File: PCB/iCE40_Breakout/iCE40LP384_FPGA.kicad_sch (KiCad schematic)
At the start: 15 parts, among them U1 ICE40LP384-SG32

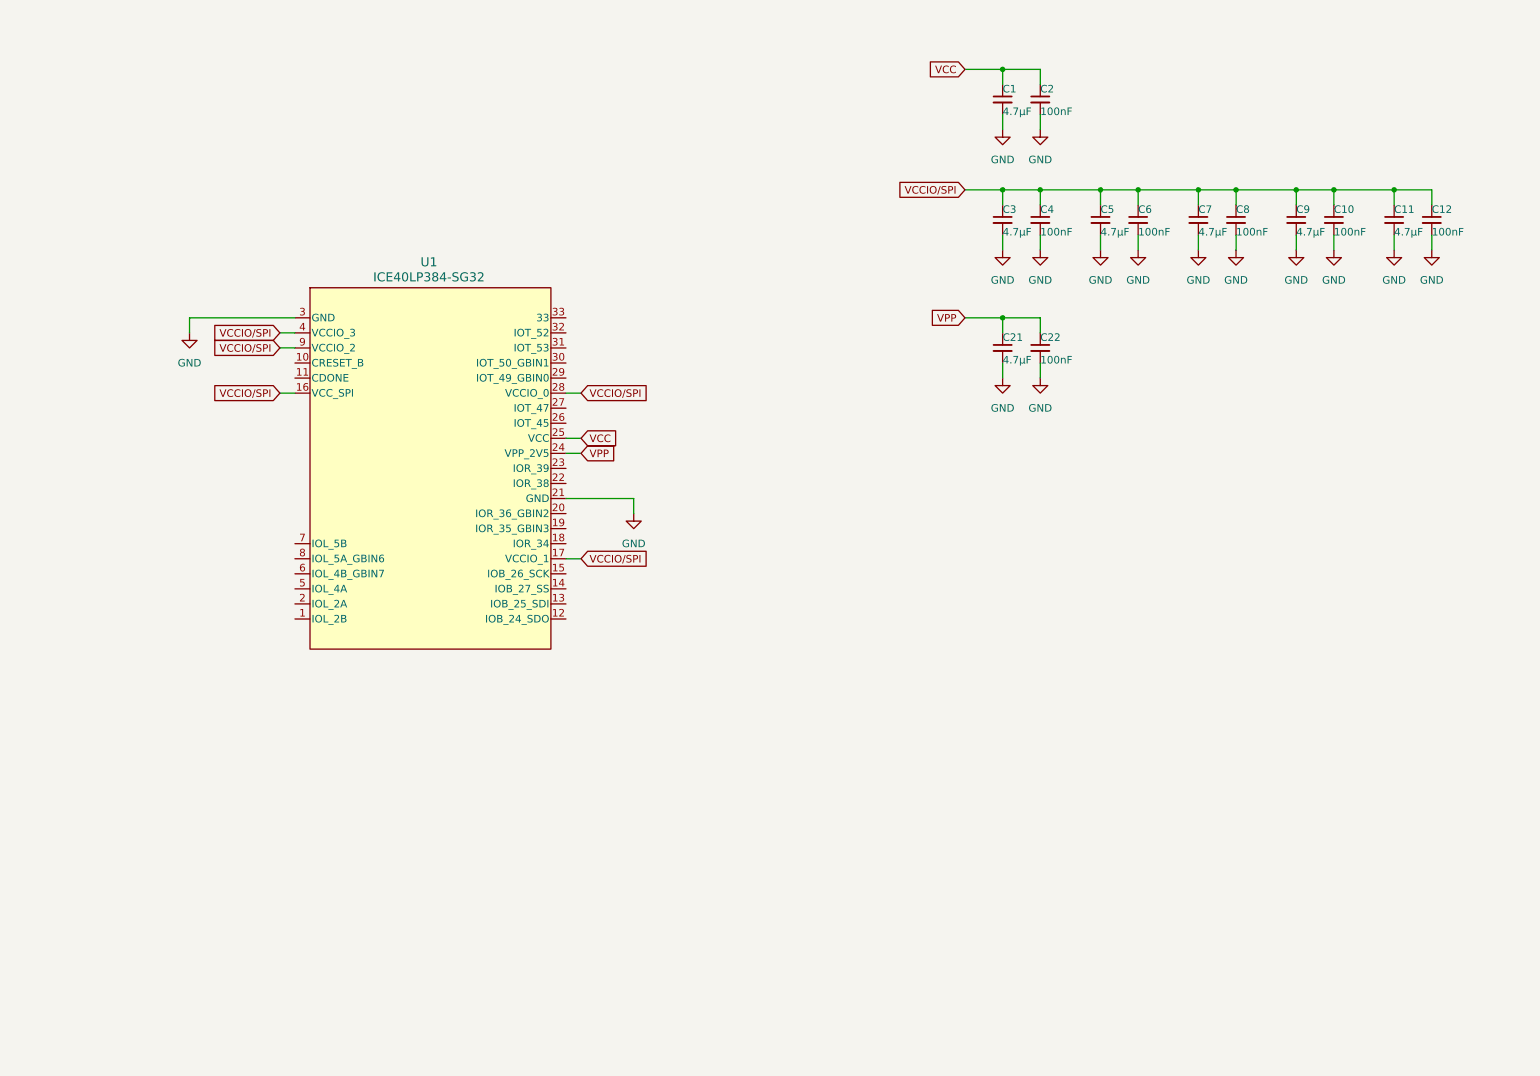
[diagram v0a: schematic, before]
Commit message: Added programming test points
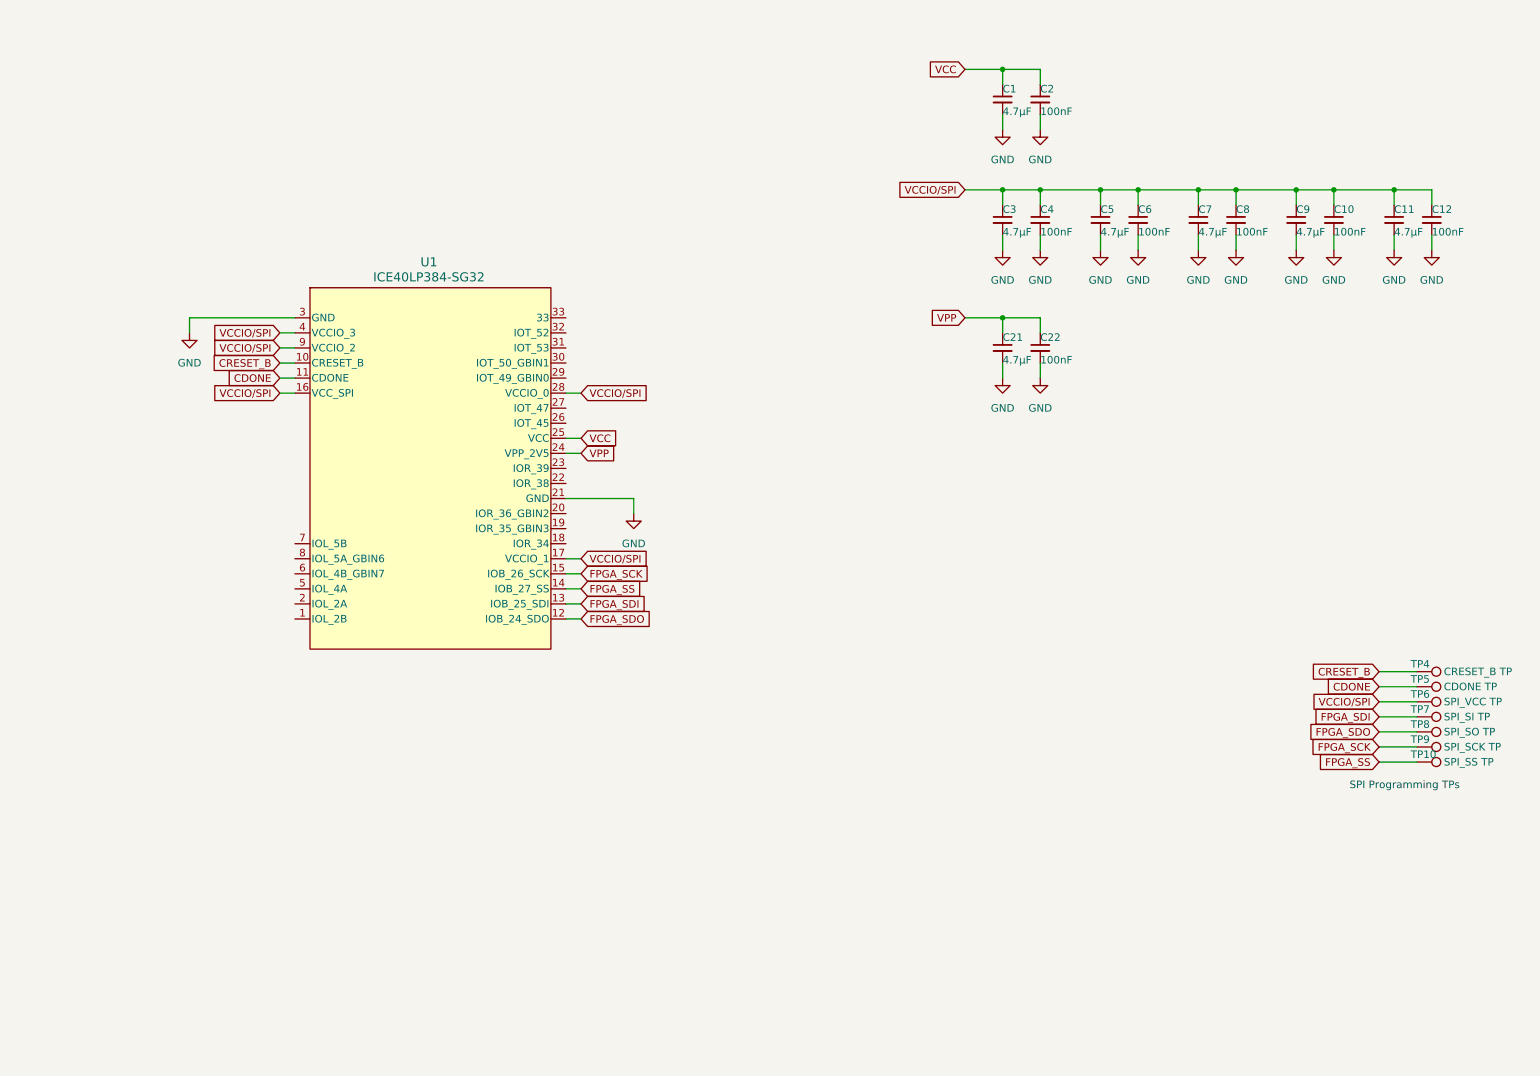
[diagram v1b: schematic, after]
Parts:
- added TP10: SPI_SS TP, symbol Connector:TestPoint
- added TP4: CRESET_B TP, symbol Connector:TestPoint
- added TP5: CDONE TP, symbol Connector:TestPoint
- added TP6: SPI_VCC TP, symbol Connector:TestPoint
- added TP7: SPI_SI TP, symbol Connector:TestPoint
- added TP8: SPI_SO TP, symbol Connector:TestPoint
- added TP9: SPI_SCK TP, symbol Connector:TestPoint
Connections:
- net VCCIO/SPI: now also TP6.1
- net CRESET_B: now reaches U1.10 (CRESET_B)
- net CRESET_B: now also TP4.1
- net CDONE: now reaches U1.11 (CDONE)
- net CDONE: now also TP5.1
- net FPGA_SDO: now reaches U1.12 (IOB_24_SDO)
- net FPGA_SDO: now also TP8.1
- net FPGA_SDI: now reaches U1.13 (IOB_25_SDI)
- net FPGA_SDI: now also TP7.1
- net FPGA_SS: now reaches U1.14 (IOB_27_SS)
- net FPGA_SS: now also TP10.1
- net FPGA_SCK: now reaches U1.15 (IOB_26_SCK)
- net FPGA_SCK: now also TP9.1
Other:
- note added: "SPI Programming TPs"

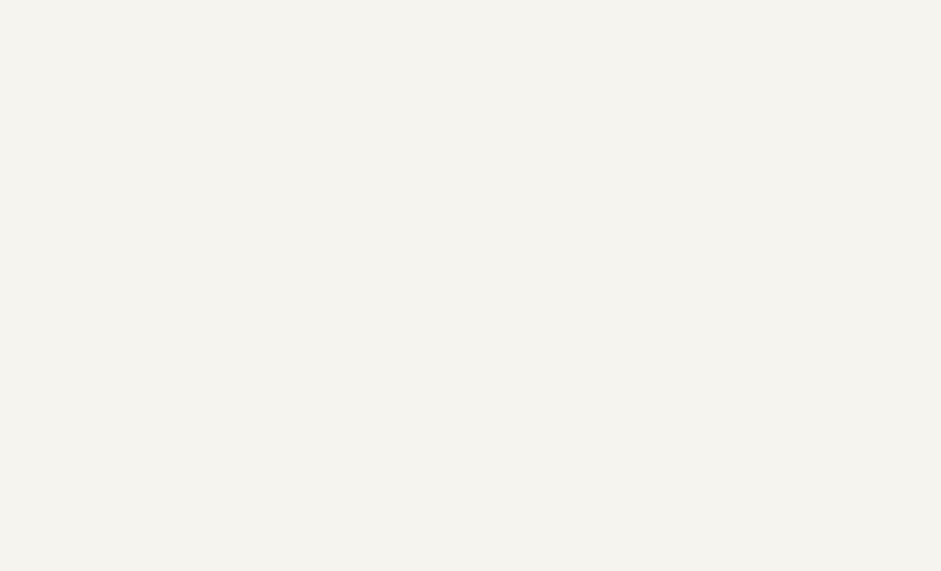
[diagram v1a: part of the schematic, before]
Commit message: Added 3V3 IO rail, reset button, and CDONE LED
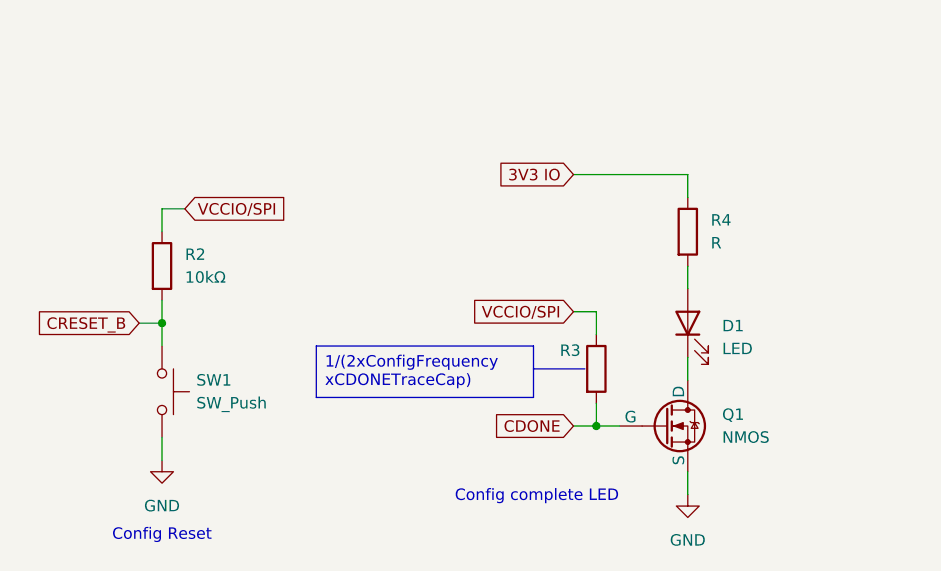
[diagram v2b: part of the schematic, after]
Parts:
- added D1: LED, symbol Device:LED
- added Q1: NMOS, symbol Simulation_SPICE:NMOS
- added R2, R3: 10kΩ, symbol Device:R
- added R4: R, symbol Device:R
- added SW1: SW_Push, symbol Switch:SW_Push
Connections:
- net CDONE: now also Q1.2 (G), R3.2
- net CRESET_B: now also R2.2, SW1.1
- net GND: now also Q1.3 (S), SW1.2
- net VCCIO/SPI: now also R2.1, R3.1
- new net: D1.1 (K), Q1.1 (D)
- new net: D1.2 (A), R4.2
- new net 3V3 IO: R4.1
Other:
- note added: "Config Reset"
- note added: "Config complete LED"

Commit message: Added footprints to all parts, and JLCPCB part numbers
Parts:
- C1, C11, C21, C3, C5, C7, C9: footprint (none) -> Capacitor_SMD:C_0402_1005Metric; LCSC (none) -> C23733
- C10, C12, C2, C22, C4, C6, C8: footprint (none) -> Capacitor_SMD:C_0402_1005Metric; LCSC (none) -> C1525
- D1: value LED -> NCD0805G1; footprint (none) -> Diode_SMD:D_0805_2012Metric; LCSC (none) -> C84260
- Q1: value NMOS -> L2N7002SLLT1G; footprint (none) -> Package_TO_SOT_SMD:SOT-23; LCSC (none) -> C22446827
- R2: footprint (none) -> Resistor_SMD:R_0603_1608Metric; LCSC (none) -> C25804
- R3: footprint (none) -> Resistor_SMD:R_0603_1608Metric
- R4: value R -> 100kΩ; footprint (none) -> Resistor_SMD:R_0603_1608Metric; LCSC (none) -> C25803
- SW1: value SW_Push -> KH-6X6X5H-STM; footprint (none) -> Button_Switch_SMD:SW_Push_1P1T_NO_E-Switch_TL3301NxxxxxG; LCSC (none) -> C2837531
- TP10, TP4, TP5, TP6, TP7, TP8, TP9: footprint (none) -> TestPoint:TestPoint_Loop_D1.80mm_Drill1.0mm_Beaded
- U1: LCSC (none) -> C2678178
